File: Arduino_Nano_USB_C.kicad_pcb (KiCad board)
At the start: 2 copper layers, 16 parts, among them J1 USB_C_Receptacle_USB2.0, J2 Conn_01x05, J3 Conn_01x05, U1 CH340G, Y1 XT9S20ANA12M

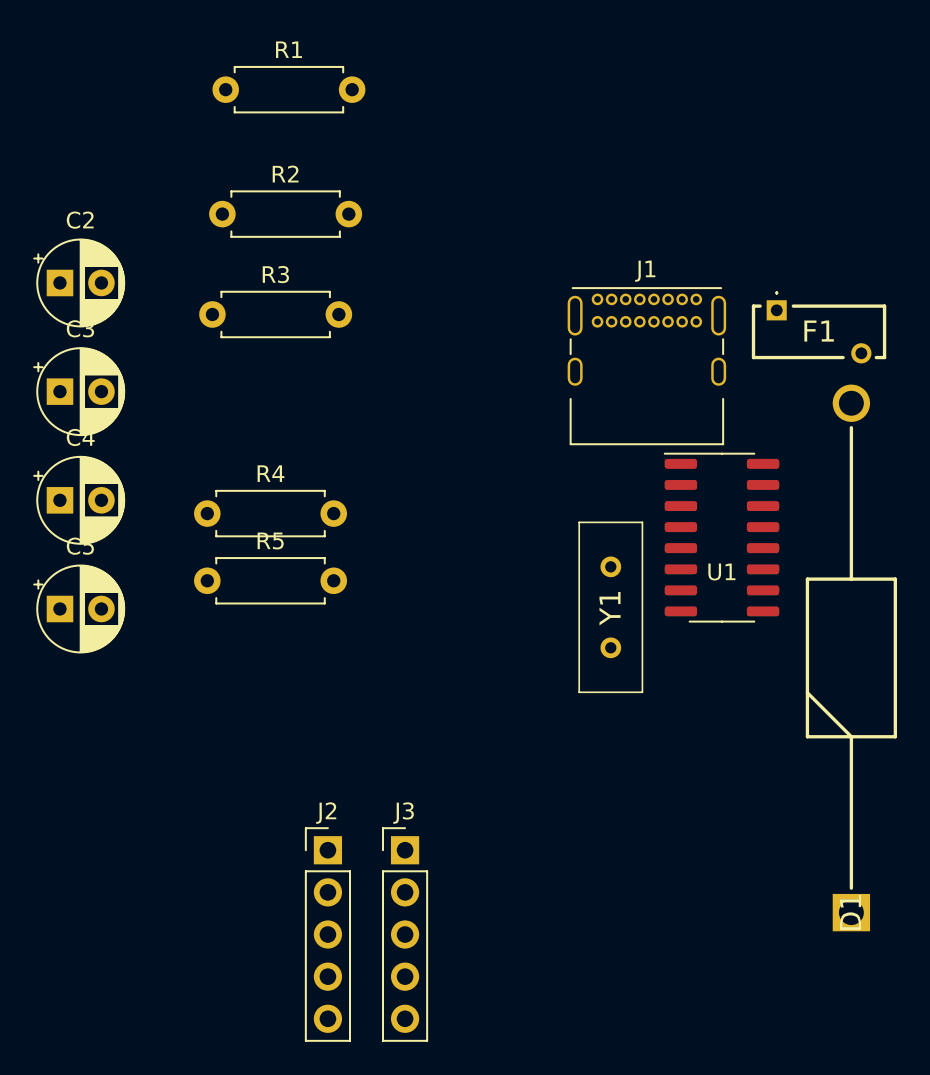
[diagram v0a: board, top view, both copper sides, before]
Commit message: Finished Layout missing Border
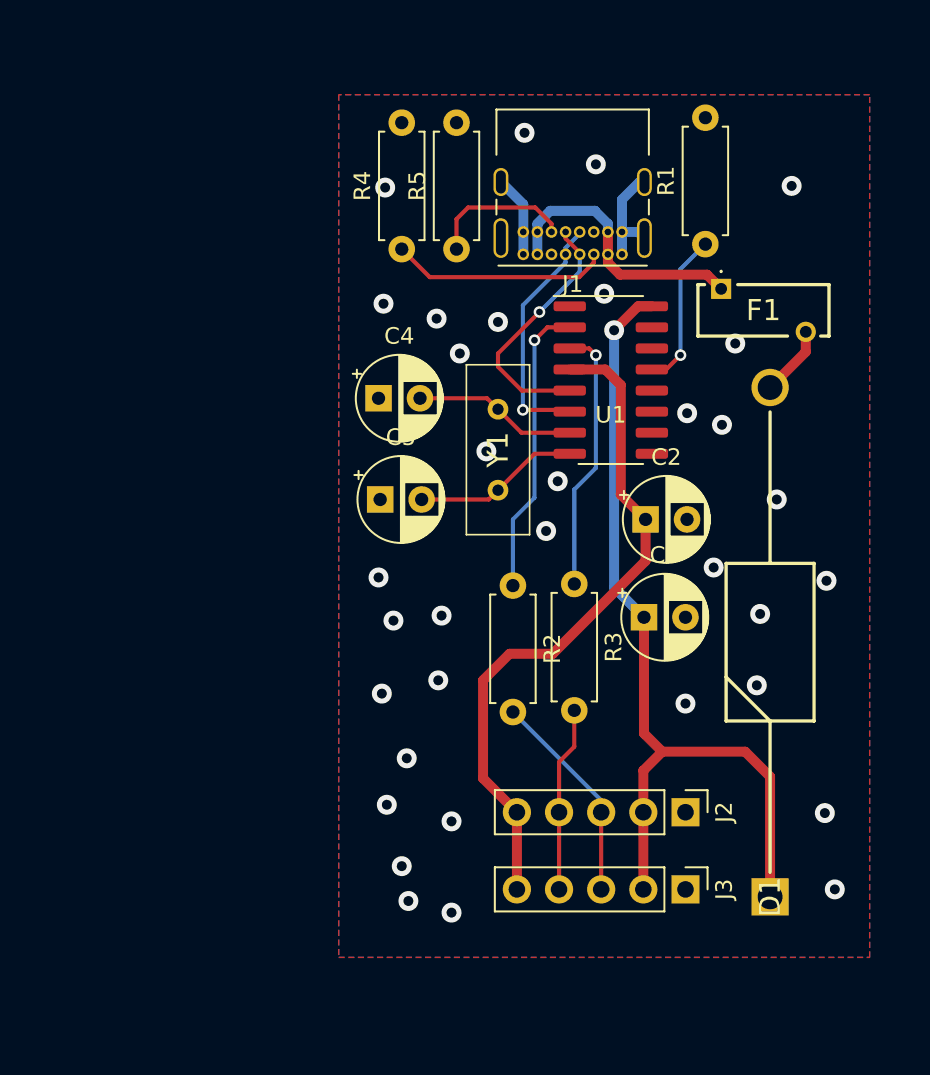
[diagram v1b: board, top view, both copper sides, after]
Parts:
- moved C2 38.1 mm to (132.5, 85.6)
- moved C3 37.7 mm to (132.4, 91.5)
- moved R1 30.4 mm to (136.1, 69.0), turned to 90 degrees
- moved R2 28.4 mm to (124.5, 89.6), turned to -90 degrees
- moved R3 27.2 mm to (128.2, 89.5), turned to -90 degrees
- moved R5 25.0 mm to (121.1, 69.3), turned to 90 degrees
- moved J2 21.7 mm to (134.9, 103.2), turned to -90 degrees
- moved C5 20.4 mm to (116.5, 84.4)
- moved C4 20.2 mm to (116.4, 78.3)
- moved R4 19.8 mm to (117.8, 69.3), turned to 90 degrees
- moved J3 17.1 mm to (134.9, 107.9), turned to -90 degrees
- moved Y1 11.7 mm to (123.6, 79.0)
- moved U1 11.6 mm to (130.4, 77.2)
- moved D1 4.99 mm to (140.0, 108.3)
- moved F1 3.59 mm to (137.1, 71.7)
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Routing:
- net +5V: track 0.00 -> 52.7 mm, vias 0 -> 1
- net +3.3V: track 0.00 -> 40.9 mm
- net Net-(U1-TXD): track 0.00 -> 17.8 mm, vias 0 -> 1
- net Net-(F1-Pad1): track 0.00 -> 16.6 mm
- net Net-(U1-RXD): track 0.00 -> 16.1 mm, vias 0 -> 1
- net Net-(U1-UD+): track 0.00 -> 15.5 mm, vias 0 -> 1
- net Net-(U1-UD-): track 0.00 -> 15.1 mm, vias 0 -> 1
- net Net-(J1-CC1): track 0.00 -> 13.1 mm
- net /Tx: track 0.00 -> 12.9 mm
- net GND: track 0.00 -> 11.5 mm, vias 0 -> 34
- net /Rx: track 0.00 -> 11.2 mm
- net Net-(U1-XO): track 0.00 -> 10.1 mm
- net Net-(U1-XI): track 0.00 -> 9.88 mm
- net Net-(U1-~{DTR}): track 0.00 -> 9.39 mm, vias 0 -> 1
- net Net-(J1-CC2): track 0.00 -> 8.73 mm
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- added copper zone on B.Cu, net GND
- added copper zone on F.Cu, net GND

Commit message: Added Edge Cute. Cleaned up Ground Plane
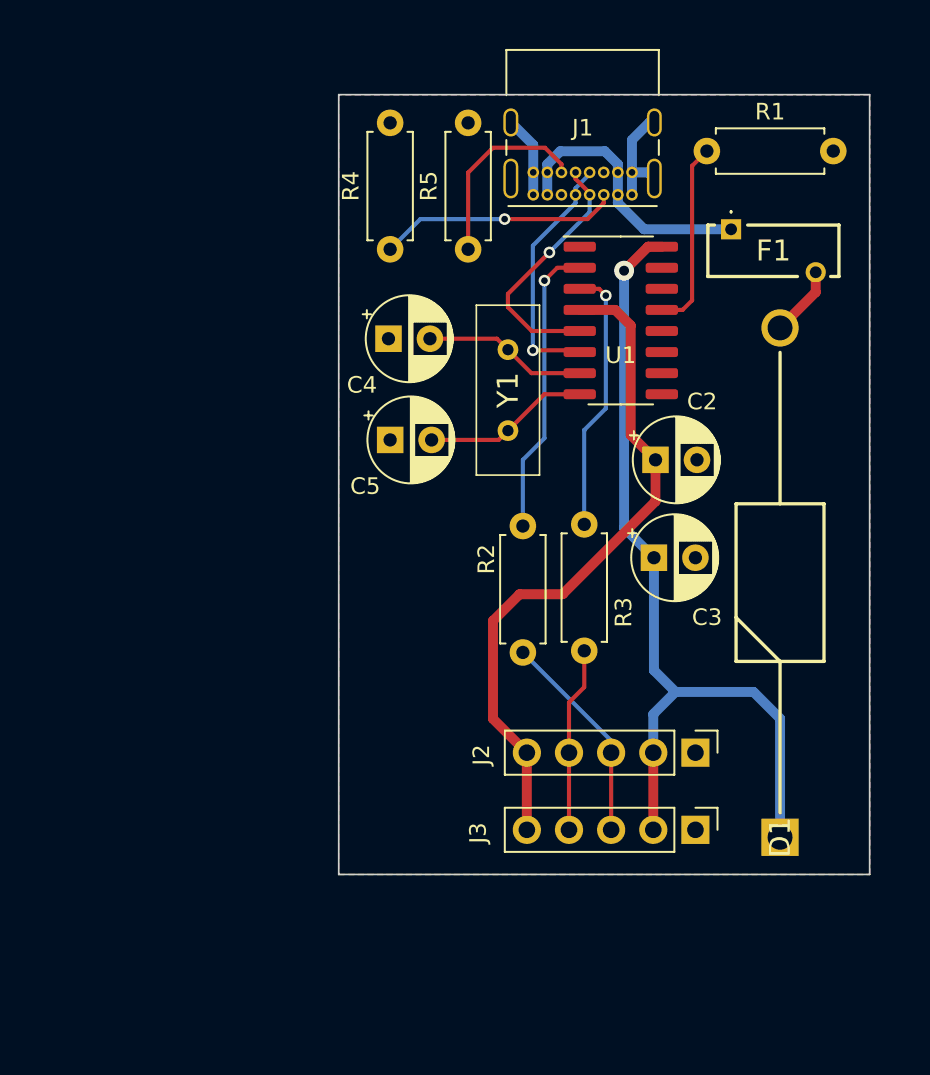
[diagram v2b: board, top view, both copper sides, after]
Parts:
- moved R1 5.61 mm to (136.2, 63.4), turned to 0 degrees
- moved J1 3.64 mm to (131.7, 66.0)
- moved C3 3.64 mm to (133.0, 87.9)
- moved C4 3.64 mm to (117.0, 74.7)
- moved C5 3.64 mm to (117.1, 80.8)
- moved F1 3.64 mm to (137.7, 68.1)
- moved J2 3.64 mm to (135.5, 99.7)
- moved J3 3.64 mm to (135.5, 104.3)
- moved R2 3.64 mm to (125.1, 86.0)
- moved U1 3.64 mm to (131.0, 73.6)
- moved R3 3.64 mm to (128.8, 85.9)
- moved Y1 3.64 mm to (124.2, 75.4)
- moved C2 3.64 mm to (133.1, 82.0)
- moved D1 3.64 mm to (140.6, 104.8)
- moved R4 0.70 mm to (117.1, 69.3)
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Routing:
- net Net-(J1-CC2): track 8.73 -> 11.8 mm
- net Net-(U1-~{DTR}): track 9.39 -> 11.4 mm, vias 1 -> 0
- net Net-(J1-CC1): track 13.1 -> 14.6 mm, vias 0 -> 1
- net GND: vias 34 -> 0
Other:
- board outline added: 32 x 47 mm

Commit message: Reordered Layout to keep decoupling capacitors close to chip. Updated pictures accordingly
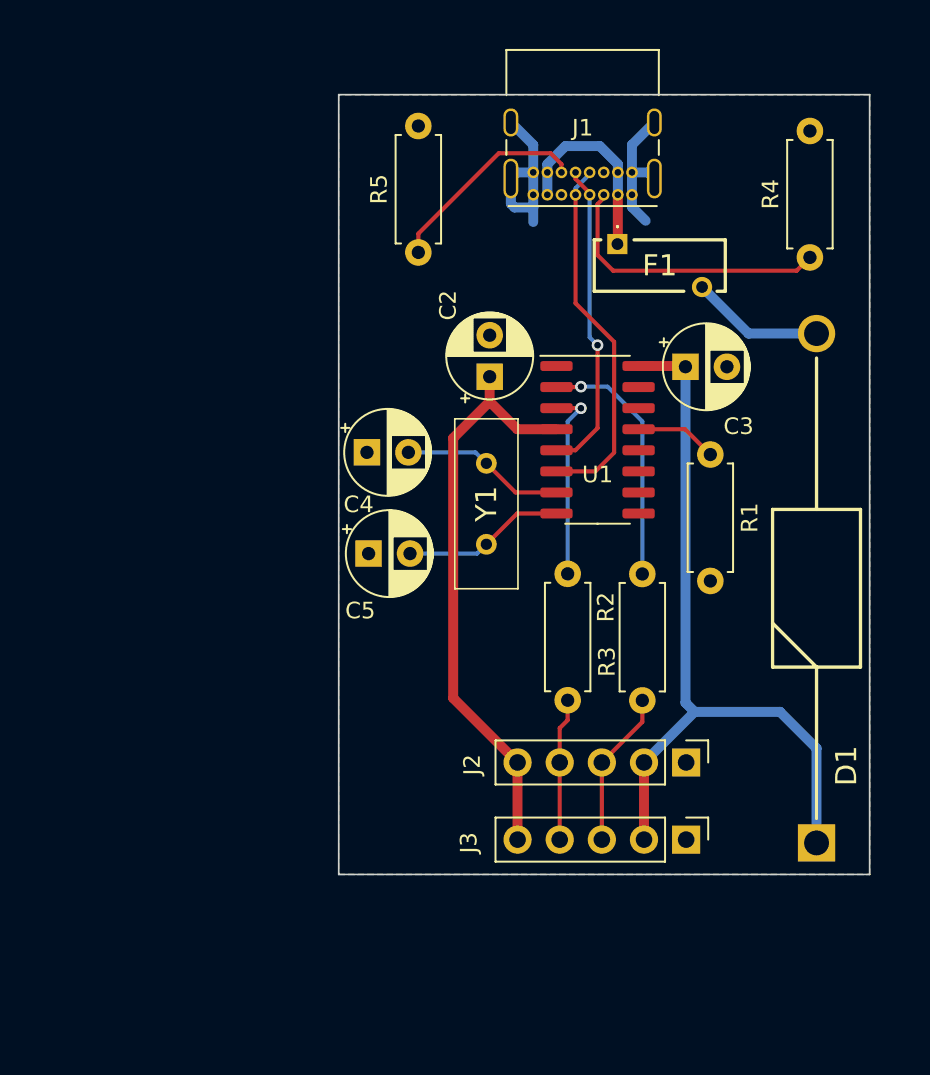
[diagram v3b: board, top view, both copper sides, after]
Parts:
- moved R4 25.3 mm to (142.4, 69.8)
- moved R1 18.3 mm to (136.4, 81.7), turned to -90 degrees
- moved C3 11.7 mm to (134.9, 76.4)
- moved C2 11.2 mm to (123.1, 77.0), turned to 90 degrees
- moved R2 7.76 mm to (132.3, 88.9)
- moved U1 7.33 mm to (129.6, 80.8)
- moved C4 6.97 mm to (115.7, 81.6)
- moved C5 6.97 mm to (115.8, 87.7)
- moved Y1 6.97 mm to (122.9, 82.2)
- moved F1 6.91 mm to (130.8, 69.0)
- moved R3 3.14 mm to (127.8, 88.9)
- moved R5 3.01 mm to (118.8, 69.5)
- moved D1 2.23 mm to (142.8, 105.1)
- moved J2 0.81 mm to (134.9, 100.2)
- moved J3 0.81 mm to (134.9, 104.9)
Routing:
- net GND: track 11.5 -> 19.4 mm
- net Net-(U1-UD-): track 15.1 -> 22.1 mm, vias 1 -> 0
- net Net-(U1-~{DTR}): track 11.4 -> 4.96 mm
- net +5V: track 52.6 -> 46.7 mm, vias 1 -> 0
- net +3.3V: track 40.9 -> 35.1 mm
- net Net-(F1-Pad1): track 16.6 -> 11.8 mm
- net Net-(U1-RXD): track 16.1 -> 11.9 mm
- net Net-(D1-A): track 4.25 -> 8.06 mm
- net /Tx: track 12.9 -> 9.40 mm
- net Net-(U1-UD+): track 15.5 -> 19.0 mm
- net Net-(J1-CC1): track 14.6 -> 17.3 mm, vias 1 -> 0
- net /Rx: track 11.2 -> 8.60 mm
- net Net-(U1-TXD): track 17.8 -> 15.4 mm
- net Net-(J1-CC2): track 11.8 -> 12.5 mm
